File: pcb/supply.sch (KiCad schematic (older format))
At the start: 10 parts

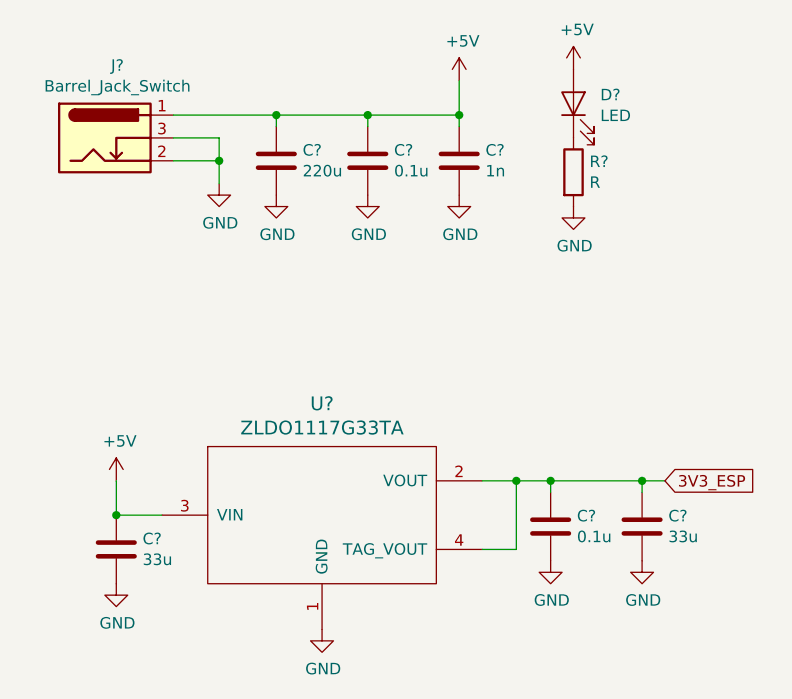
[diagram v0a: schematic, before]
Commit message: RTC to PCB
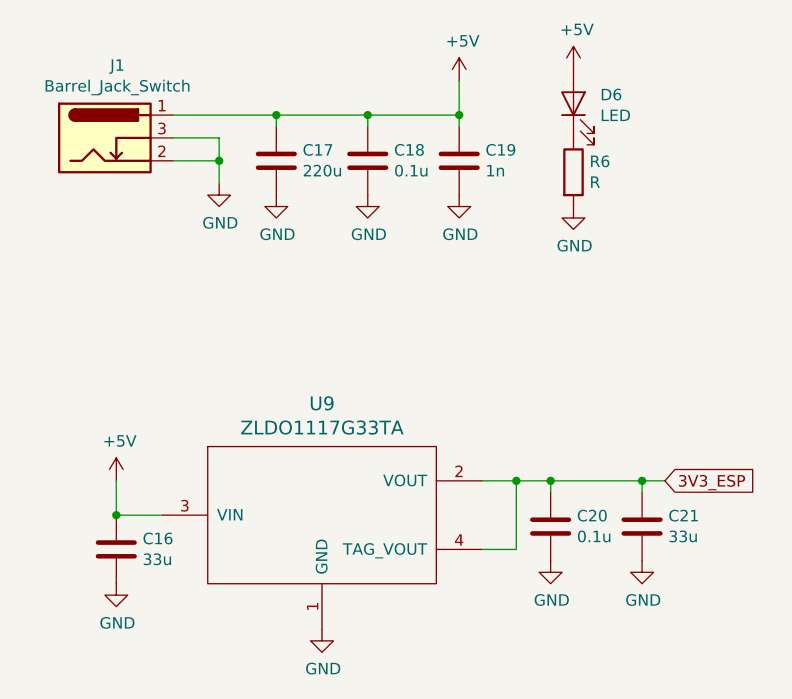
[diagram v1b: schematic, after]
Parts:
- gave numbers to parts that had none: 10
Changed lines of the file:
@@
 P 1700 1950
 AR Path="/5E909FE7" Ref="J?"  Part="1"
-AR Path="/5E8E60A3/5E909FE7" Ref="J?"  Part="1"
-F 0 "J?" H 1755 2267 50  0000 C CNN
+AR Path="/5E8E60A3/5E909FE7" Ref="J1"  Part="1"
+F 0 "J1" H 1755 2267 50  0000 C CNN
 F 1 "Barrel_Jack_Switch" H 1755 2176 50  0000 C CNN
 F 2 "" H 1750 1910 50  0001 C CNN
@@
 	2200 2050 2000 2050
 $Comp
-L power:GND #PWR?
+L power:GND #PWR0106
 U 1 1 5E90A075
 P 2200 2150
-F 0 "#PWR?" H 2200 1900 50  0001 C CNN
+F 0 "#PWR0106" H 2200 1900 50  0001 C CNN
 F 1 "GND" H 2205 1977 50  0000 C CNN
 F 2 "" H 2200 2150 50  0001 C CNN
@@
 Connection ~ 2200 2050
 $Comp
-L Device:C C?
+L Device:C C17
 U 1 1 5E90A0C5
 P 2450 2050
-F 0 "C?" H 2565 2096 50  0000 L CNN
+F 0 "C17" H 2565 2096 50  0000 L CNN
 F 1 "220u" H 2565 2005 50  0000 L CNN
 F 2 "" H 2488 1900 50  0001 C CNN
@@
 $EndComp
 $Comp
-L Device:C C?
+L Device:C C18
 U 1 1 5E90A0EF
 P 2850 2050
-F 0 "C?" H 2965 2096 50  0000 L CNN
+F 0 "C18" H 2965 2096 50  0000 L CNN
 F 1 "0.1u" H 2965 2005 50  0000 L CNN
 F 2 "" H 2888 1900 50  0001 C CNN
@@
 $EndComp
 $Comp
-L Device:C C?
+L Device:C C19
 U 1 1 5E90A112
 P 3250 2050
-F 0 "C?" H 3365 2096 50  0000 L CNN
+F 0 "C19" H 3365 2096 50  0000 L CNN
 F 1 "1n" H 3365 2005 50  0000 L CNN
 F 2 "" H 3288 1900 50  0001 C CNN
@@
 	2450 1850 2850 1850
 $Comp
-L power:GND #PWR?
+L power:GND #PWR0107
 U 1 1 5E90A3AB
 P 2450 2200
-F 0 "#PWR?" H 2450 1950 50  0001 C CNN
+F 0 "#PWR0107" H 2450 1950 50  0001 C CNN
 F 1 "GND" H 2455 2027 50  0000 C CNN
 F 2 "" H 2450 2200 50  0001 C CNN
@@
 $EndComp
 $Comp
-L power:GND #PWR?
+L power:GND #PWR0108
 U 1 1 5E90A3D9
 P 2850 2200
-F 0 "#PWR?" H 2850 1950 50  0001 C CNN
+F 0 "#PWR0108" H 2850 1950 50  0001 C CNN
 F 1 "GND" H 2855 2027 50  0000 C CNN
 F 2 "" H 2850 2200 50  0001 C CNN
@@
 $EndComp
 $Comp
-L power:GND #PWR?
+L power:GND #PWR0109
 U 1 1 5E90A407
 P 3250 2200
-F 0 "#PWR?" H 3250 1950 50  0001 C CNN
+F 0 "#PWR0109" H 3250 1950 50  0001 C CNN
 F 1 "GND" H 3255 2027 50  0000 C CNN
 F 2 "" H 3250 2200 50  0001 C CNN
@@
 $EndComp
 $Comp
-L power:+5V #PWR?
+L power:+5V #PWR0110
 U 1 1 5E90A470
 P 3250 1700
-F 0 "#PWR?" H 3250 1550 50  0001 C CNN
+F 0 "#PWR0110" H 3250 1550 50  0001 C CNN
 F 1 "+5V" H 3265 1873 50  0000 C CNN
 F 2 "" H 3250 1700 50  0001 C CNN
@@
 Connection ~ 3250 1850
 $Comp
-L Device:LED D?
+L Device:LED D6
 U 1 1 5E9039A0
 P 3750 1800
-F 0 "D?" V 3788 1683 50  0000 R CNN
+F 0 "D6" V 3788 1683 50  0000 R CNN
 F 1 "LED" V 3697 1683 50  0000 R CNN
 F 2 "" H 3750 1800 50  0001 C CNN
@@
 $EndComp
 $Comp
-L power:+5V #PWR?
+L power:+5V #PWR0111
 U 1 1 5E903AFE
 P 3750 1650
-F 0 "#PWR?" H 3750 1500 50  0001 C CNN
+F 0 "#PWR0111" H 3750 1500 50  0001 C CNN
 F 1 "+5V" H 3765 1823 50  0000 C CNN
 F 2 "" H 3750 1650 50  0001 C CNN
@@
 $EndComp
 $Comp
-L Device:R R?
+L Device:R R6
 U 1 1 5E903B44
 P 3750 2100
-F 0 "R?" H 3820 2146 50  0000 L CNN
+F 0 "R6" H 3820 2146 50  0000 L CNN
 F 1 "R" H 3820 2055 50  0000 L CNN
 F 2 "" V 3680 2100 50  0001 C CNN
@@
 $EndComp
 $Comp
-L power:GND #PWR?
+L power:GND #PWR0112
 U 1 1 5E903C05
 P 3750 2250
-F 0 "#PWR?" H 3750 2000 50  0001 C CNN
+F 0 "#PWR0112" H 3750 2000 50  0001 C CNN
 F 1 "GND" H 3755 2077 50  0000 C CNN
 F 2 "" H 3750 2250 50  0001 C CNN
@@
 $EndComp
 $Comp
-L ZLDO1117G33TA:ZLDO1117G33TA U?
+L ZLDO1117G33TA:ZLDO1117G33TA U9
 U 1 1 5E8F23ED
 P 2650 3600
-F 0 "U?" H 2650 4087 60  0000 C CNN
+F 0 "U9" H 2650 4087 60  0000 C CNN
 F 1 "ZLDO1117G33TA" H 2650 3981 60  0000 C CNN
 F 2 "" H 2800 3650 60  0000 C CNN
@@
 $EndComp
 $Comp
-L power:+5V #PWR?
+L power:+5V #PWR0116
 U 1 1 5E8F2677
 P 1750 3450
-F 0 "#PWR?" H 1750 3300 50  0001 C CNN
+F 0 "#PWR0116" H 1750 3300 50  0001 C CNN
 F 1 "+5V" H 1765 3623 50  0000 C CNN
 F 2 "" H 1750 3450 50  0001 C CNN
@@
 $EndComp
 $Comp
-L power:GND #PWR?
+L power:GND #PWR0117
 U 1 1 5E8F2717
 P 2650 4100
-F 0 "#PWR?" H 2650 3850 50  0001 C CNN
+F 0 "#PWR0117" H 2650 3850 50  0001 C CNN
 F 1 "GND" H 2655 3927 50  0000 C CNN
 F 2 "" H 2650 4100 50  0001 C CNN
@@
 Connection ~ 3500 3450
 $Comp
-L Device:C C?
+L Device:C C20
 U 1 1 5E8F4D80
 P 3650 3650
-F 0 "C?" H 3765 3696 50  0000 L CNN
+F 0 "C20" H 3765 3696 50  0000 L CNN
 F 1 "0.1u" H 3765 3605 50  0000 L CNN
 F 2 "" H 3688 3500 50  0001 C CNN
@@
 $EndComp
 $Comp
-L Device:C C?
+L Device:C C21
 U 1 1 5E8F4DD0
 P 4050 3650
-F 0 "C?" H 4165 3696 50  0000 L CNN
+F 0 "C21" H 4165 3696 50  0000 L CNN
 F 1 "33u" H 4165 3605 50  0000 L CNN
 F 2 "" H 4088 3500 50  0001 C CNN
@@
 $EndComp
 $Comp
-L Device:C C?
+L Device:C C16
 U 1 1 5E8F4E66
 P 1750 3750
-F 0 "C?" H 1865 3796 50  0000 L CNN
+F 0 "C16" H 1865 3796 50  0000 L CNN
 F 1 "33u" H 1865 3705 50  0000 L CNN
 F 2 "" H 1788 3600 50  0001 C CNN
@@
 	4050 3450 3650 3450
 $Comp
-L power:GND #PWR?
+L power:GND #PWR0119
 U 1 1 5E8F5816
 P 1750 3900
-F 0 "#PWR?" H 1750 3650 50  0001 C CNN
+F 0 "#PWR0119" H 1750 3650 50  0001 C CNN
 F 1 "GND" H 1755 3727 50  0000 C CNN
 F 2 "" H 1750 3900 50  0001 C CNN
@@
 $EndComp
 $Comp
-L power:GND #PWR?
+L power:GND #PWR0120
 U 1 1 5E8F58EC
 P 3650 3800
-F 0 "#PWR?" H 3650 3550 50  0001 C CNN
+F 0 "#PWR0120" H 3650 3550 50  0001 C CNN
 F 1 "GND" H 3655 3627 50  0000 C CNN
 F 2 "" H 3650 3800 50  0001 C CNN
@@
 $EndComp
 $Comp
-L power:GND #PWR?
+L power:GND #PWR0131
 U 1 1 5E8F592C
 P 4050 3800
-F 0 "#PWR?" H 4050 3550 50  0001 C CNN
+F 0 "#PWR0131" H 4050 3550 50  0001 C CNN
 F 1 "GND" H 4055 3627 50  0000 C CNN
 F 2 "" H 4050 3800 50  0001 C CNN

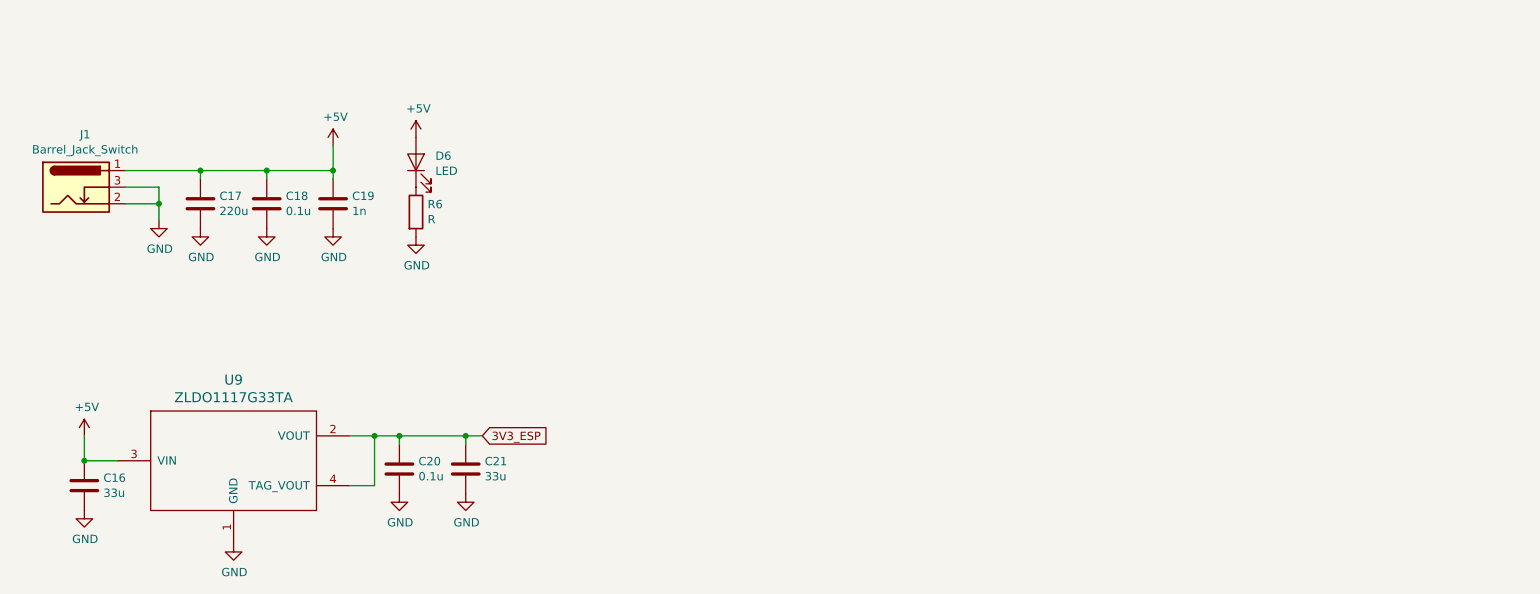
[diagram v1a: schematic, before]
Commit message: added miscellaneous to electro valves sheet
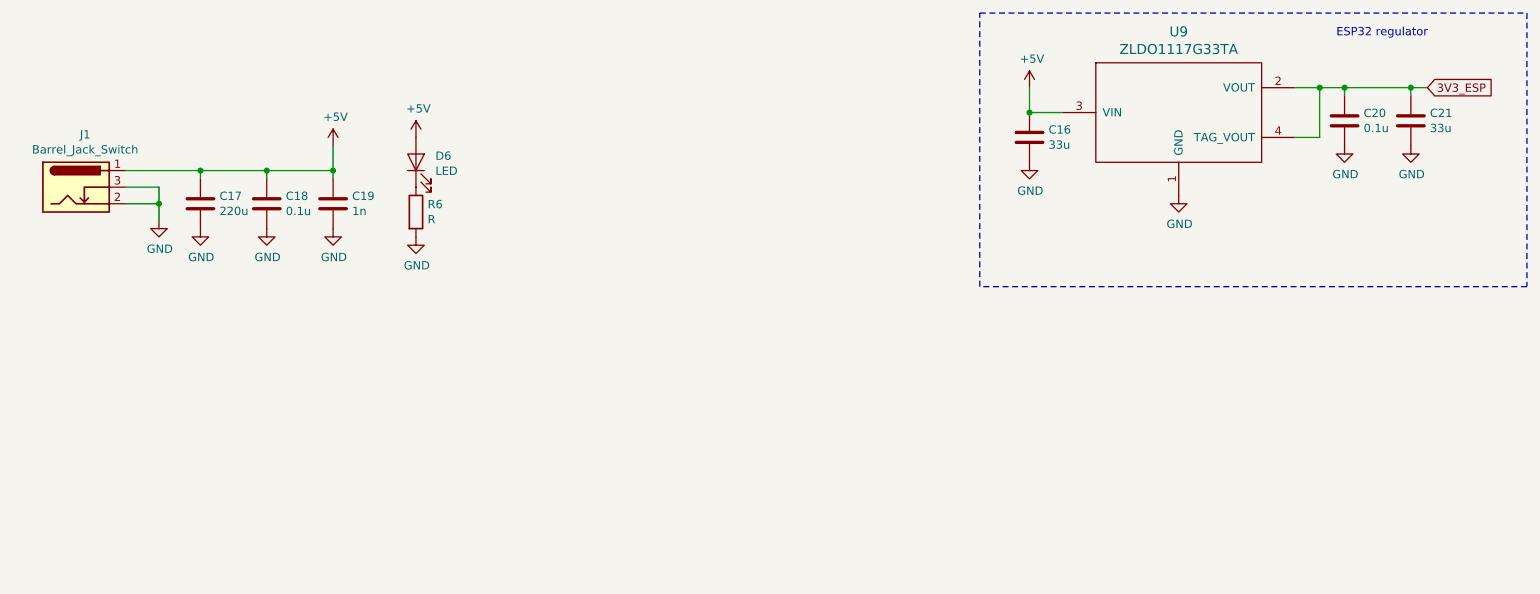
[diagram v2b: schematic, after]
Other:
- note added: "ESP32 regulator\n"
- moved on the sheet: C16, C20, C21, U9
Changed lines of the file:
@@
 EESchema Schematic File Version 4
 LIBS:keep_breathing_ctrl-cache
-EELAYER 30 0
+EELAYER 26 0
 EELAYER END
 $Descr A4 11693 8268
@@
 L ZLDO1117G33TA:ZLDO1117G33TA U9
 U 1 1 5E8F23ED
-P 2650 3600
-F 0 "U9" H 2650 4087 60  0000 C CNN
-F 1 "ZLDO1117G33TA" H 2650 3981 60  0000 C CNN
-F 2 "" H 2800 3650 60  0000 C CNN
-F 3 "https://www.diodes.com/assets/Datasheets/ZLDO1117.pdf" H 2650 3981 60  0001 C CNN
-F 4 "ZLDO1117G33DICT-ND" H 2650 3600 50  0001 C CNN "Digikey"
-	1    2650 3600
+P 8350 1500
+F 0 "U9" H 8350 1987 60  0000 C CNN
+F 1 "ZLDO1117G33TA" H 8350 1881 60  0000 C CNN
+F 2 "" H 8500 1550 60  0000 C CNN
+F 3 "https://www.diodes.com/assets/Datasheets/ZLDO1117.pdf" H 8350 1881 60  0001 C CNN
+F 4 "ZLDO1117G33DICT-ND" H 8350 1500 50  0001 C CNN "Digikey"
+	1    8350 1500
 	1    0    0    -1
 $EndComp
@@
 L power:+5V #PWR0116
 U 1 1 5E8F2677
-P 1750 3450
-F 0 "#PWR0116" H 1750 3300 50  0001 C CNN
-F 1 "+5V" H 1765 3623 50  0000 C CNN
-F 2 "" H 1750 3450 50  0001 C CNN
-F 3 "" H 1750 3450 50  0001 C CNN
-	1    1750 3450
+P 7450 1350
+F 0 "#PWR0116" H 7450 1200 50  0001 C CNN
+F 1 "+5V" H 7465 1523 50  0000 C CNN
+F 2 "" H 7450 1350 50  0001 C CNN
+F 3 "" H 7450 1350 50  0001 C CNN
+	1    7450 1350
 	1    0    0    -1
 $EndComp
@@
 L power:GND #PWR0117
 U 1 1 5E8F2717
-P 2650 4100
-F 0 "#PWR0117" H 2650 3850 50  0001 C CNN
-F 1 "GND" H 2655 3927 50  0000 C CNN
-F 2 "" H 2650 4100 50  0001 C CNN
-F 3 "" H 2650 4100 50  0001 C CNN
-	1    2650 4100
-	1    0    0    -1
-$EndComp
-Wire Wire Line
-	3350 3750 3500 3750
-Wire Wire Line
-	3500 3750 3500 3450
-Wire Wire Line
-	3500 3450 3350 3450
-Text GLabel 4150 3450 2    50   Input ~ 0
+P 8350 2000
+F 0 "#PWR0117" H 8350 1750 50  0001 C CNN
+F 1 "GND" H 8355 1827 50  0000 C CNN
+F 2 "" H 8350 2000 50  0001 C CNN
+F 3 "" H 8350 2000 50  0001 C CNN
+	1    8350 2000
+	1    0    0    -1
+$EndComp
+Wire Wire Line
+	9050 1650 9200 1650
+Wire Wire Line
+	9200 1650 9200 1350
+Wire Wire Line
+	9200 1350 9050 1350
+Text GLabel 9850 1350 2    50   Input ~ 0
 3V3_ESP
 Wire Wire Line
-	4150 3450 4050 3450
-Connection ~ 3500 3450
+	9850 1350 9750 1350
+Connection ~ 9200 1350
 $Comp
 L Device:C C20
 U 1 1 5E8F4D80
-P 3650 3650
-F 0 "C20" H 3765 3696 50  0000 L CNN
-F 1 "0.1u" H 3765 3605 50  0000 L CNN
-F 2 "" H 3688 3500 50  0001 C CNN
-F 3 "~" H 3650 3650 50  0001 C CNN
-	1    3650 3650
+P 9350 1550
+F 0 "C20" H 9465 1596 50  0000 L CNN
+F 1 "0.1u" H 9465 1505 50  0000 L CNN
+F 2 "" H 9388 1400 50  0001 C CNN
+F 3 "~" H 9350 1550 50  0001 C CNN
+	1    9350 1550
 	1    0    0    -1
 $EndComp
@@
 L Device:C C21
 U 1 1 5E8F4DD0
-P 4050 3650
-F 0 "C21" H 4165 3696 50  0000 L CNN
-F 1 "33u" H 4165 3605 50  0000 L CNN
-F 2 "" H 4088 3500 50  0001 C CNN
-F 3 "~" H 4050 3650 50  0001 C CNN
-	1    4050 3650
+P 9750 1550
+F 0 "C21" H 9865 1596 50  0000 L CNN
+F 1 "33u" H 9865 1505 50  0000 L CNN
+F 2 "" H 9788 1400 50  0001 C CNN
+F 3 "~" H 9750 1550 50  0001 C CNN
+	1    9750 1550
 	1    0    0    -1
 $EndComp
@@
 L Device:C C16
 U 1 1 5E8F4E66
-P 1750 3750
-F 0 "C16" H 1865 3796 50  0000 L CNN
-F 1 "33u" H 1865 3705 50  0000 L CNN
-F 2 "" H 1788 3600 50  0001 C CNN
-F 3 "~" H 1750 3750 50  0001 C CNN
-	1    1750 3750
-	1    0    0    -1
-$EndComp
-Wire Wire Line
-	1950 3600 1750 3600
-Wire Wire Line
-	1750 3450 1750 3600
-Connection ~ 1750 3600
-Wire Wire Line
-	3650 3500 3650 3450
-Connection ~ 3650 3450
-Wire Wire Line
-	3650 3450 3500 3450
-Wire Wire Line
-	4050 3500 4050 3450
-Connection ~ 4050 3450
-Wire Wire Line
-	4050 3450 3650 3450
+P 7450 1650
+F 0 "C16" H 7565 1696 50  0000 L CNN
+F 1 "33u" H 7565 1605 50  0000 L CNN
+F 2 "" H 7488 1500 50  0001 C CNN
+F 3 "~" H 7450 1650 50  0001 C CNN
+	1    7450 1650
+	1    0    0    -1
+$EndComp
+Wire Wire Line
+	7650 1500 7450 1500
+Wire Wire Line
+	7450 1350 7450 1500
+Connection ~ 7450 1500
+Wire Wire Line
+	9350 1400 9350 1350
+Connection ~ 9350 1350
+Wire Wire Line
+	9350 1350 9200 1350
+Wire Wire Line
+	9750 1400 9750 1350
+Connection ~ 9750 1350
+Wire Wire Line
+	9750 1350 9350 1350
 $Comp
 L power:GND #PWR0119
 U 1 1 5E8F5816
-P 1750 3900
-F 0 "#PWR0119" H 1750 3650 50  0001 C CNN
-F 1 "GND" H 1755 3727 50  0000 C CNN
-F 2 "" H 1750 3900 50  0001 C CNN
-F 3 "" H 1750 3900 50  0001 C CNN
-	1    1750 3900
+P 7450 1800
+F 0 "#PWR0119" H 7450 1550 50  0001 C CNN
+F 1 "GND" H 7455 1627 50  0000 C CNN
+F 2 "" H 7450 1800 50  0001 C CNN
+F 3 "" H 7450 1800 50  0001 C CNN
+	1    7450 1800
 	1    0    0    -1
 $EndComp
@@
 L power:GND #PWR0120
 U 1 1 5E8F58EC
-P 3650 3800
-F 0 "#PWR0120" H 3650 3550 50  0001 C CNN
-F 1 "GND" H 3655 3627 50  0000 C CNN
-F 2 "" H 3650 3800 50  0001 C CNN
-F 3 "" H 3650 3800 50  0001 C CNN
-	1    3650 3800
+P 9350 1700
+F 0 "#PWR0120" H 9350 1450 50  0001 C CNN
+F 1 "GND" H 9355 1527 50  0000 C CNN
+F 2 "" H 9350 1700 50  0001 C CNN
+F 3 "" H 9350 1700 50  0001 C CNN
+	1    9350 1700
 	1    0    0    -1
 $EndComp
@@
 L power:GND #PWR0131
 U 1 1 5E8F592C
-P 4050 3800
-F 0 "#PWR0131" H 4050 3550 50  0001 C CNN
-F 1 "GND" H 4055 3627 50  0000 C CNN
-F 2 "" H 4050 3800 50  0001 C CNN
-F 3 "" H 4050 3800 50  0001 C CNN
-	1    4050 3800
-	1    0    0    -1
-$EndComp
+P 9750 1700
+F 0 "#PWR0131" H 9750 1450 50  0001 C CNN
+F 1 "GND" H 9755 1527 50  0000 C CNN
+F 2 "" H 9750 1700 50  0001 C CNN
+F 3 "" H 9750 1700 50  0001 C CNN
+	1    9750 1700
+	1    0    0    -1
+$EndComp
+Wire Notes Line
+	7150 900  10450 900
+Wire Notes Line
+	10450 900  10450 2550
+Wire Notes Line
+	10450 2550 7150 2550
+Wire Notes Line
+	7150 2550 7150 900
+Text Notes 9300 1050 0    50   ~ 0
+ESP32 regulator\n
 $EndSCHEMATC

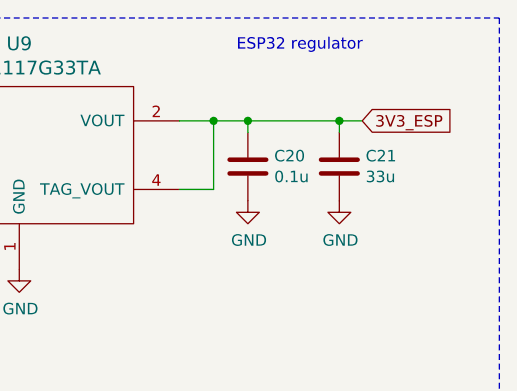
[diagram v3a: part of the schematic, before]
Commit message: connecting esp32 signals
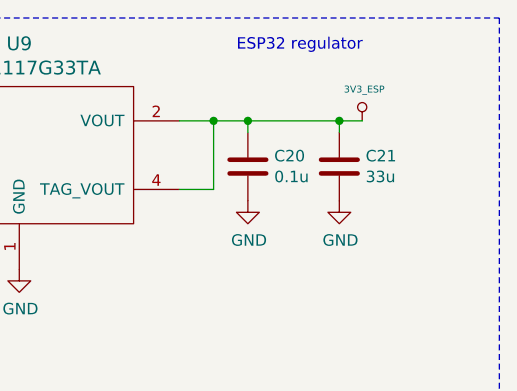
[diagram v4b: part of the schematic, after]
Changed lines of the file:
@@
 Wire Wire Line
 	9200 1350 9050 1350
-Text GLabel 9850 1350 2    50   Input ~ 0
-3V3_ESP
 Wire Wire Line
 	9850 1350 9750 1350
@@
 Text Notes 9300 1050 0    50   ~ 0
 ESP32 regulator\n
+$Comp
+L ventilator-PowerSymbols:3V3_ESP #PWR0165
+U 1 1 5E9883BE
+P 9850 1350
+F 0 "#PWR0165" H 9850 1310 30  0001 C CNN
+F 1 "3V3_ESP" H 9859 1488 30  0000 C CNN
+F 2 "" H 9850 1350 60  0000 C CNN
+F 3 "" H 9850 1350 60  0000 C CNN
+	1    9850 1350
+	1    0    0    -1
+$EndComp
 $EndSCHEMATC

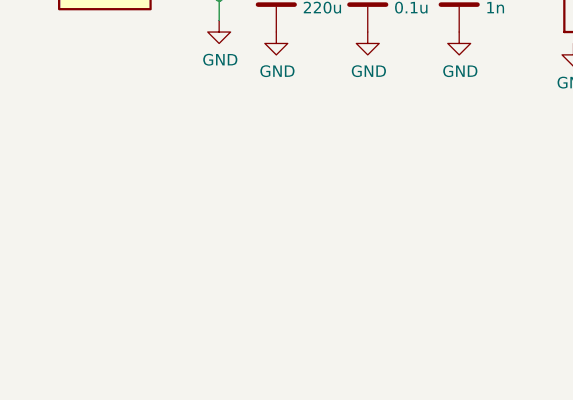
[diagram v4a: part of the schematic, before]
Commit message: added connections to ElectroValves sheet
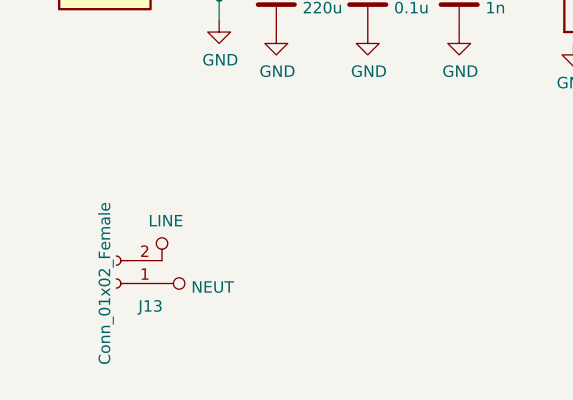
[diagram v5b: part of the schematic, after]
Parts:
- added J13: Conn_01x02_Female, symbol BarrelConnector:Conn_01x02_Female
- J1: footprint (none) -> TH:BARREL_JACK
- U9: footprint (none) -> SMD:SOT-223
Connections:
- new net LINE: J13.2 (Pin_2)
- new net NEUT: J13.1 (Pin_1)
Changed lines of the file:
@@
 EESchema Schematic File Version 4
 LIBS:keep_breathing_ctrl-cache
-EELAYER 30 0
+EELAYER 26 0
 EELAYER END
 $Descr A4 11693 8268
@@
 F 0 "J1" H 1755 2267 50  0000 C CNN
 F 1 "Barrel_Jack_Switch" H 1755 2176 50  0000 C CNN
-F 2 "" H 1750 1910 50  0001 C CNN
+F 2 "TH:BARREL_JACK" H 1750 1910 50  0001 C CNN
 F 3 "~" H 1750 1910 50  0001 C CNN
 	1    1700 1950
@@
 F 0 "U9" H 8350 1987 60  0000 C CNN
 F 1 "ZLDO1117G33TA" H 8350 1881 60  0000 C CNN
-F 2 "" H 8500 1550 60  0000 C CNN
+F 2 "SMD:SOT-223" H 8500 1550 60  0001 C CNN
 F 3 "https://www.diodes.com/assets/Datasheets/ZLDO1117.pdf" H 8350 1881 60  0001 C CNN
 F 4 "ZLDO1117G33DICT-ND" H 8350 1500 50  0001 C CNN "Digikey"
@@
 	1    0    0    -1
 $EndComp
+$Comp
+L BarrelConnector:Conn_01x02_Female J13
+U 1 1 5E9D6DF1
+P 1750 3300
+F 0 "J13" H 1600 3400 50  0000 C CNN
+F 1 "Conn_01x02_Female" V 1800 3300 50  0000 C CNN
+F 2 "" H 1750 3300 50  0001 C CNN
+F 3 "~" H 1750 3300 50  0001 C CNN
+	1    1750 3300
+	-1   0    0    1
+$EndComp
+$Comp
+L power:LINE #PWR019
+U 1 1 5E9D6F84
+P 1950 3200
+F 0 "#PWR019" H 1950 3050 50  0001 C CNN
+F 1 "LINE" H 1967 3373 50  0000 C CNN
+F 2 "" H 1950 3200 50  0001 C CNN
+F 3 "" H 1950 3200 50  0001 C CNN
+	1    1950 3200
+	1    0    0    -1
+$EndComp
+$Comp
+L power:NEUT #PWR020
+U 1 1 5E9D7006
+P 1950 3300
+F 0 "#PWR020" H 1950 3150 50  0001 C CNN
+F 1 "NEUT" V 1967 3428 50  0000 L CNN
+F 2 "" H 1950 3300 50  0001 C CNN
+F 3 "" H 1950 3300 50  0001 C CNN
+	1    1950 3300
+	0    1    1    0
+$EndComp
 $EndSCHEMATC
